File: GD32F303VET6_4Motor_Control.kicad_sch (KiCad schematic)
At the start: 0 parts

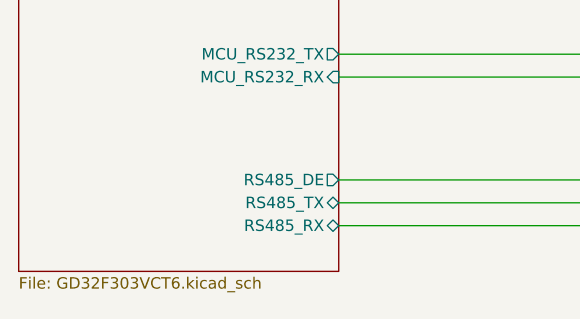
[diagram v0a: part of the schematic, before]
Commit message: 重命名为GD32F303VET6四电机驱动控制板
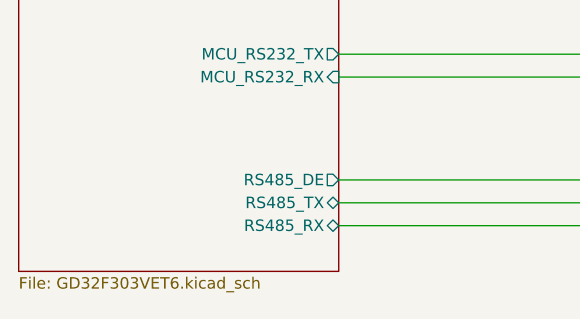
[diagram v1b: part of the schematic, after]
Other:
- sheet MCU_Core: file GD32F303VCT6.kicad_sch -> GD32F303VET6.kicad_sch
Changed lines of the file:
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@@
 		)
 		(instances
-			(project "GD32F303"
+			(project "GD32F303VET6_4Motor_Control"
 				(path "/54005433-e3aa-4693-8f75-bb73943288d3"
 					(page "6")
@@
 		)
 		(instances
-			(project "GD32F303"
+			(project "GD32F303VET6_4Motor_Control"
 				(path "/54005433-e3aa-4693-8f75-bb73943288d3"
 					(page "4")
@@
 		)
 		(instances
-			(project "GD32F303"
+			(project "GD32F303VET6_4Motor_Control"
 				(path "/54005433-e3aa-4693-8f75-bb73943288d3"
 					(page "5")
@@
 		)
 		(instances
-			(project "GD32F303"
+			(project "GD32F303VET6_4Motor_Control"
 				(path "/54005433-e3aa-4693-8f75-bb73943288d3"
 					(page "2")
@@
 			)
 		)
-		(property "Sheetfile" "GD32F303VCT6.kicad_sch"
+		(property "Sheetfile" "GD32F303VET6.kicad_sch"
 			(at 128.27 149.1746 0)
 			(show_name no)
@@
 		)
 		(instances
-			(project "GD32F303"
+			(project "GD32F303VET6_4Motor_Control"
 				(path "/54005433-e3aa-4693-8f75-bb73943288d3"
 					(page "3")

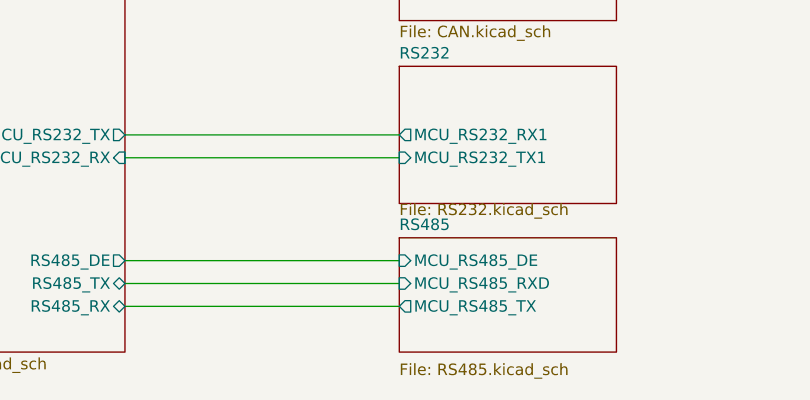
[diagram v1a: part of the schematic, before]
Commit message: 更新六层电机控制板设计与器件库
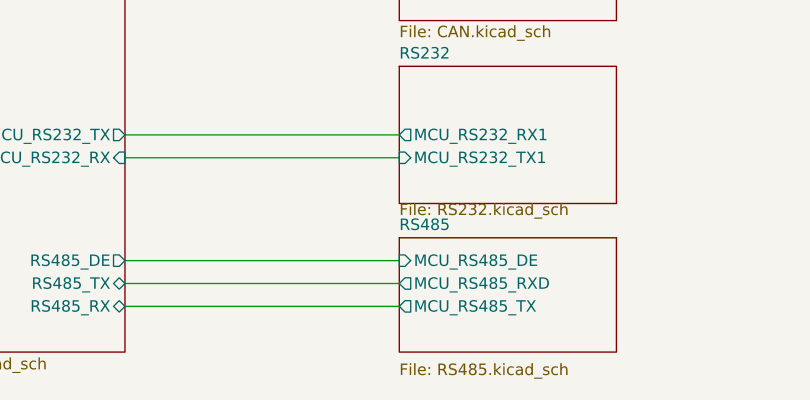
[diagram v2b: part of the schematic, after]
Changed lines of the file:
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@@
 			)
 		)
-		(pin "MCU_RS485_RXD" input
+		(pin "MCU_RS485_RXD" output
 			(at 194.31 140.97 180)
 			(effects

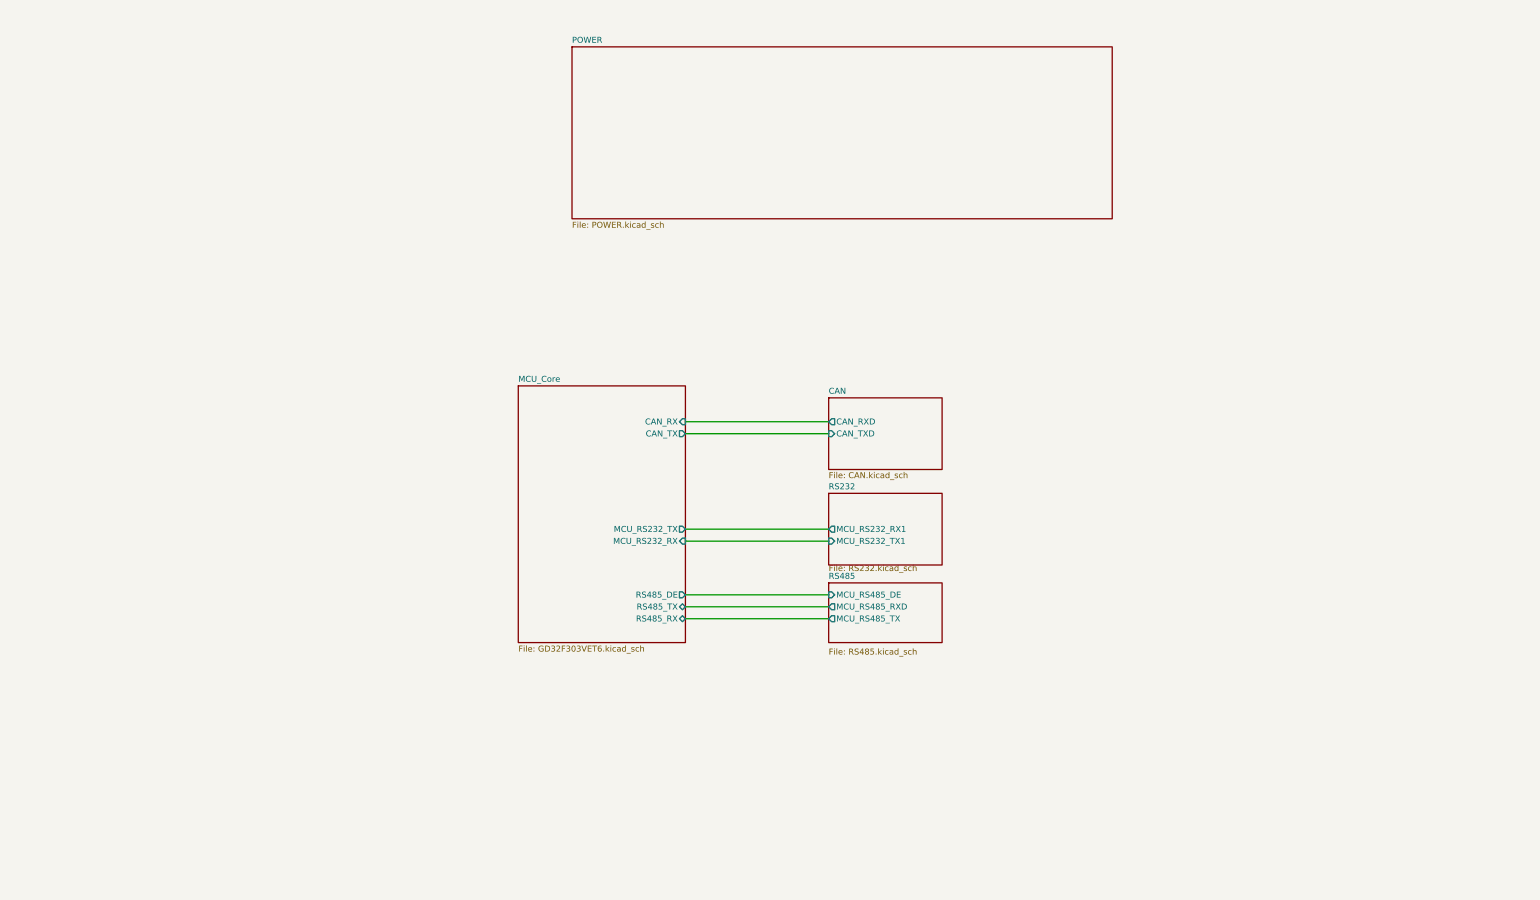
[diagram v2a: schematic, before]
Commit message: V2.0: sync KiCad design, add firmware snapshot and README
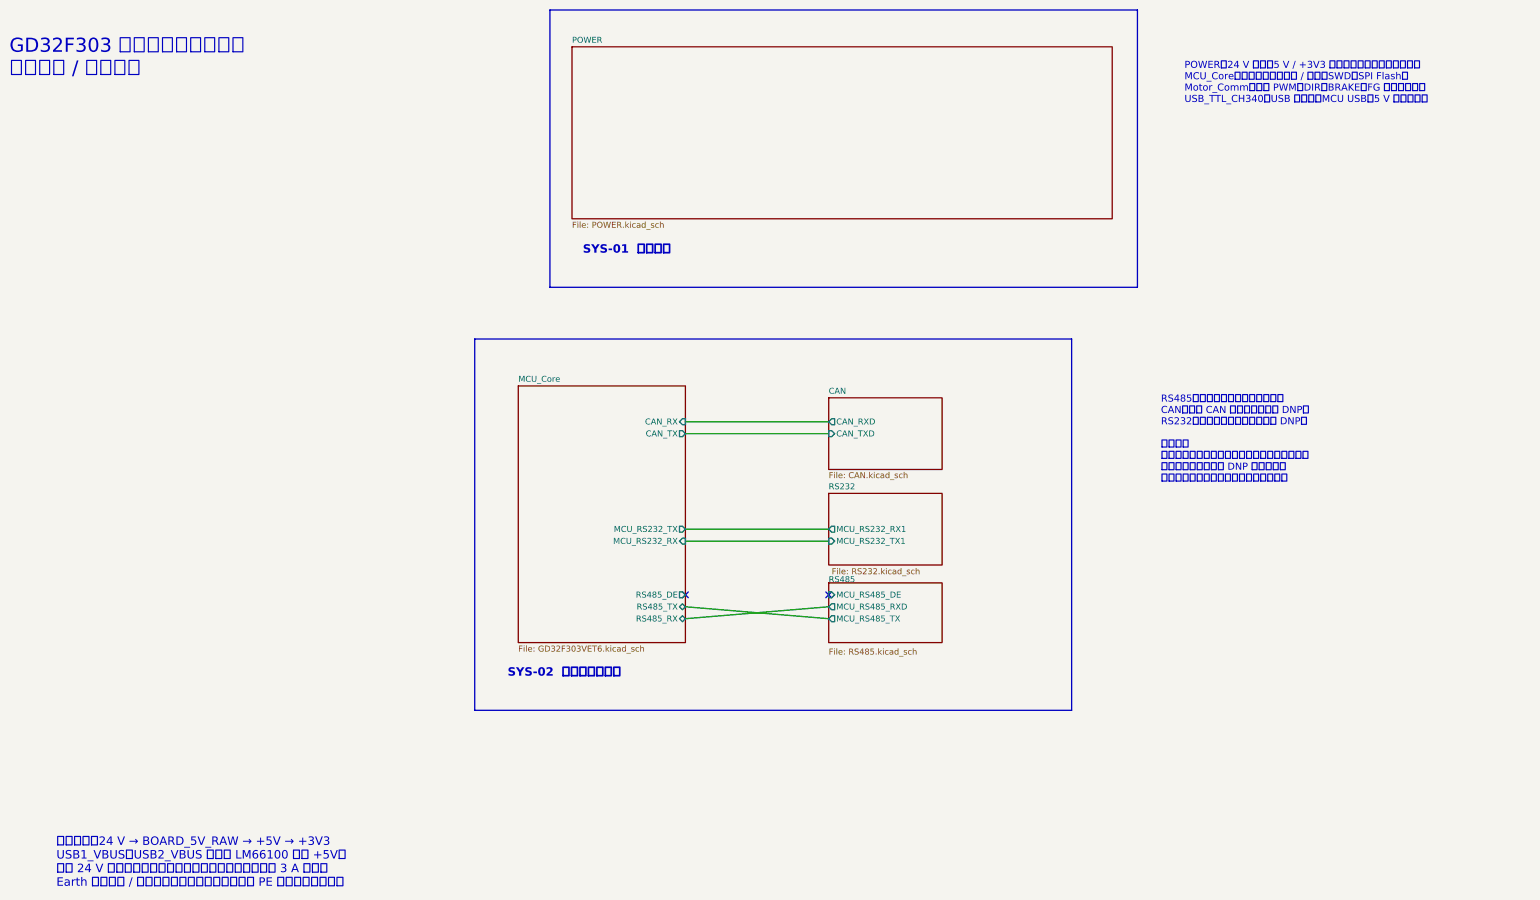
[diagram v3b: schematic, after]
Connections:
- no-connect marks 0 -> 2
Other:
- note added: "GD32F303 四路无刷电机控制板 系统总览 / 功能分区"
- note added: "POWER：24 V 输入、5 V / +3V3 电源、供电指示、机壳连接。 MCU_Core：主控、时钟、启动 / 复位、SWD、SPI Flash。 Motor_Comm：四路 PWM、DIR、BRAKE、FG 与电机接口。 USB_TTL_CH340：USB 转串口、MCU USB、5 V 电源汇合。"
- note added: "RS485：当前装配的自动收发接口。 CAN：隔离 CAN 备用电路，当前 DNP。 RS232：电平转换备用电路，当前 DNP。 阅读约定 实线框：功能分区；虚线框：备用不装配区域。 具体装配状态以元件 DNP 属性为准。 分区编号仅用于阅读，不改变网络连接。"
- note added: "SYS-01 电源系统"
- note added: "SYS-02 主控与通信互联"
- note added: "供电路径：24 V → BOARD_5V_RAW → +5V → +3V3 USB1_VBUS、USB2_VBUS 经各自 LM66100 接入 +5V。 电机 24 V 回路与控制板共地；四路电机合计最大电流按 3 A 设计。 Earth 表示机壳 / 金属安装板网络，是否接保护地 PE 由整机接线决定。"
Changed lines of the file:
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@@
 	(generator_version "10.0")
 	(paper "A3")
-	(wire
-		(pts
-			(xy 163.83 143.51) (xy 194.31 143.51)
-		)
-		(stroke
-			(width 0)
-			(type default)
-		)
+	(rectangle
+		(start 135 14)
+		(end 260 73)
+		(stroke
+			(width 0.254)
+			(type solid)
+		)
+		(fill
+			(type none)
+		)
+	)
+	(rectangle
+		(start 119 84)
+		(end 246 163)
+		(stroke
+			(width 0.254)
+			(type solid)
+		)
+		(fill
+			(type none)
+		)
+	)
+	(text "GD32F303 四路无刷电机控制板\n系统总览 / 功能分区"
+		(exclude_from_sim no)
+		(at 20 20 0)
+		(effects
+			(font
+				(face "宋体")
+				(size 3 3)
+			)
+			(justify left top)
+		)
+	)
+	(text "SYS-02  主控与通信互联"
+		(exclude_from_sim no)
+		(at 126 154 0)
+		(effects
+			(font
+				(face "宋体")
+				(size 1.8 1.8)
+				(bold yes)
+			)
+			(justify left top)
+		)
+	)
+	(text "供电路径：24 V → BOARD_5V_RAW → +5V → +3V3\nUSB1_VBUS、USB2_VBUS 经各自 LM66100 接入 +5V。\n电机 24 V 回路与控制板共地；四路电机合计最大电流按 3 A 设计。\nEarth 表示机壳 / 金属安装板网络，是否接保护地 PE 由整机接线决定。"
+		(exclude_from_sim no)
+		(at 30 190 0)
+		(effects
+			(font
+				(face "宋体")
+				(size 1.8 1.8)
+			)
+			(justify left top)
+		)
+	)
+	(text "POWER：24 V 输入、5 V / +3V3 电源、供电指示、机壳连接。\nMCU_Core：主控、时钟、启动 / 复位、SWD、SPI Flash。\nMotor_Comm：四路 PWM、DIR、BRAKE、FG 与电机接口。\nUSB_TTL_CH340：USB 转串口、MCU USB、5 V 电源汇合。"
+		(exclude_from_sim no)
+		(at 270 25 0)
+		(effects
+			(font
+				(face "宋体")
+				(size 1.5 1.5)
+			)
+			(justify left top)
+		)
+	)
+	(text "SYS-01  电源系统"
+		(exclude_from_sim no)
+		(at 142 64 0)
+		(effects
+			(font
+				(face "宋体")
+				(size 1.8 1.8)
+				(bold yes)
+			)
+			(justify left top)
+		)
+	)
+	(text "RS485：当前装配的自动收发接口。\nCAN：隔离 CAN 备用电路，当前 DNP。\nRS232：电平转换备用电路，当前 DNP。\n\n阅读约定\n实线框：功能分区；虚线框：备用不装配区域。\n具体装配状态以元件 DNP 属性为准。\n分区编号仅用于阅读，不改变网络连接。"
+		(exclude_from_sim no)
+		(at 265 96 0)
+		(effects
+			(font
+				(face "宋体")
+				(size 1.5 1.5)
+			)
+			(justify left top)
+		)
+	)
+	(no_connect
+		(at 163.83 138.43)
+	)
+	(no_connect
+		(at 194.31 138.43)
 	)
 	(wire
@@
 	(wire
 		(pts
+			(xy 194.31 140.97) (xy 163.83 143.51)
+		)
+		(stroke
+			(width 0)
+			(type default)
+		)
+	)
+	(wire
+		(pts
 			(xy 194.31 101.6) (xy 163.83 101.6)
 		)
@@
 	(wire
 		(pts
-			(xy 163.83 140.97) (xy 194.31 140.97)
-		)
-		(stroke
-			(width 0)
-			(type default)
-		)
-	)
-	(wire
-		(pts
 			(xy 163.83 104.14) (xy 194.31 104.14)
 		)
@@
 	(wire
 		(pts
-			(xy 163.83 138.43) (xy 194.31 138.43)
+			(xy 163.83 140.97) (xy 194.31 143.51)
 		)
 		(stroke
@@
 		(on_board yes)
 		(dnp no)
-		(fields_autoplaced yes)
 		(stroke
 			(width 0.1524)
@@
 		)
 		(property "Sheetname" "RS485"
-			(at 194.31 135.1784 0)
+			(at 194.31 135.89 0)
 			(show_name no)
 			(do_not_autoplace no)
@@
 		(on_board yes)
 		(dnp no)
-		(fields_autoplaced yes)
 		(stroke
 			(width 0.1524)
@@
 		)
 		(property "Sheetfile" "RS232.kicad_sch"
-			(at 194.31 132.0296 0)
-			(show_name no)
-			(do_not_autoplace no)
+			(at 194.945 132.715 0)
+			(show_name no)
+			(do_not_autoplace no)

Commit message: 更新V2.0电路设计及0.5oz内层制造交付资料
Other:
- note added: "24V → BOARD_5V_RAW → +5V → +3V3。 USB1_VBUS / USB2_VBUS 经各自 LM66100 汇入 +5V。 四路电机合计最大电流按 3A；控制与电机共地。 Earth 为机壳 / 金属安装板网络，是否连接 PE 由整机接线决定。"
- note added: "GD32F303 四路电机控制板 系统功能目录"
- note added: "POWER：24V 输入、5V / 3V3、电源指示、Earth。 MCU_Core：主控、时钟、复位、SWD、SPI Flash。 Motor_Comm：四路 PWM、DIR、BRAKE、FG。 新增 MOT-08：PA15 可编程 LED，低电平亮。 USB_TTL_CH340：串口桥、原生 USB、供电汇合。 CH340 使用 USART2：PD8 TX / PD9 RX。 RS485：USART1 自动收发，共地接口。 CAN / RS232：保留电路，当前不装配。 WiFi_OTA：备用不装配，USART0 / PA9、PA10。 实线：功能分区；虚线：备用 DNP。 具体装配及 PCB 排除状态以元件属性为准。 注释说明当前接线，不代表电气验收通过。"
- note added: "SYS-02 主控与总线接口"
- note added: "SYS-03 功能目录与装配状态"
- note added: "SYS-04 供电与接地路径"
- note removed: "GD32F303 四路无刷电机控制板 系统总览 / 功能分区"
- note removed: "POWER：24 V 输入、5 V / +3V3 电源、供电指示、机壳连接。 MCU_Core：主控、时钟、启动 / 复位、SWD、SPI Flash。 Motor_Comm：四路 PWM、DIR、BRAKE、FG 与电机接口。 USB_TTL_CH340：USB 转串口、MCU USB、5 V 电源汇合。"
- note removed: "RS485：当前装配的自动收发接口。 CAN：隔离 CAN 备用电路，当前 DNP。 RS232：电平转换备用电路，当前 DNP。 阅读约定 实线框：功能分区；虚线框：备用不装配区域。 具体装配状态以元件 DNP 属性为准。 分区编号仅用于阅读，不改变网络连接。"
- note removed: "SYS-02 主控与通信互联"
- note removed: "供电路径：24 V → BOARD_5V_RAW → +5V → +3V3 USB1_VBUS、USB2_VBUS 经各自 LM66100 接入 +5V。 电机 24 V 回路与控制板共地；四路电机合计最大电流按 3 A 设计。 Earth 表示机壳 / 金属安装板网络，是否接保护地 PE 由整机接线决定。"
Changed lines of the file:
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@@
+	)
+	(rectangle
+		(start 20 175)
+		(end 265 221)
+		(stroke
+			(width 0.254)
+			(type solid)
+		)
+		(fill
+			(type none)
+		)
 	)
 	(rectangle
@@
 		)
 	)
-	(text "GD32F303 四路无刷电机控制板\n系统总览 / 功能分区"
+	(rectangle
+		(start 265 14)
+		(end 405 164)
+		(stroke
+			(width 0.254)
+			(type solid)
+		)
+		(fill
+			(type none)
+		)
+	)
+	(text "POWER：24V 输入、5V / 3V3、电源指示、Earth。\nMCU_Core：主控、时钟、复位、SWD、SPI Flash。\nMotor_Comm：四路 PWM、DIR、BRAKE、FG。\n新增 MOT-08：PA15 可编程 LED，低电平亮。\nUSB_TTL_CH340：串口桥、原生 USB、供电汇合。\nCH340 使用 USART2：PD8 TX / PD9 RX。\nRS485：USART1 自动收发，共地接口。\nCAN / RS232：保留电路，当前不装配。\nWiFi_OTA：备用不装配，USART0 / PA9、PA10。\n\n实线：功能分区；虚线：备用 DNP。\n具体装配及 PCB 排除状态以元件属性为准。\n注释说明当前接线，不代表电气验收通过。"
 		(exclude_from_sim no)
-		(at 20 20 0)
+		(at 270 27 0)
 		(effects
 			(font
-				(face "宋体")
-				(size 3 3)
+				(face "Microsoft YaHei")
+				(size 1.8 1.8)
 			)
 			(justify left top)
 		)
 	)
-	(text "SYS-02  主控与通信互联"
+	(text "SYS-04  供电与接地路径"
 		(exclude_from_sim no)
-		(at 126 154 0)
+		(at 23 178 0)
 		(effects
 			(font
-				(face "宋体")
-				(size 1.8 1.8)
+				(face "Microsoft YaHei")
+				(size 2 2)
 				(bold yes)
 			)
@@
 		)
 	)
-	(text "供电路径：24 V → BOARD_5V_RAW → +5V → +3V3\nUSB1_VBUS、USB2_VBUS 经各自 LM66100 接入 +5V。\n电机 24 V 回路与控制板共地；四路电机合计最大电流按 3 A 设计。\nEarth 表示机壳 / 金属安装板网络，是否接保护地 PE 由整机接线决定。"
+	(text "24V → BOARD_5V_RAW → +5V → +3V3。\nUSB1_VBUS / USB2_VBUS 经各自 LM66100 汇入 +5V。\n四路电机合计最大电流按 3A；控制与电机共地。\nEarth 为机壳 / 金属安装板网络，是否连接 PE 由整机接线决定。"
 		(exclude_from_sim no)
-		(at 30 190 0)
+		(at 25 187 0)
 		(effects
 			(font
-				(face "宋体")
+				(face "Microsoft YaHei")
 				(size 1.8 1.8)
-			)
-			(justify left top)
-		)
-	)
-	(text "POWER：24 V 输入、5 V / +3V3 电源、供电指示、机壳连接。\nMCU_Core：主控、时钟、启动 / 复位、SWD、SPI Flash。\nMotor_Comm：四路 PWM、DIR、BRAKE、FG 与电机接口。\nUSB_TTL_CH340：USB 转串口、MCU USB、5 V 电源汇合。"
-		(exclude_from_sim no)
-		(at 270 25 0)
-		(effects
-			(font
-				(face "宋体")
-				(size 1.5 1.5)
 			)
 			(justify left top)
@@
 	(text "SYS-01  电源系统"
 		(exclude_from_sim no)
-		(at 142 64 0)
+		(at 141 64 0)
 		(effects
 			(font
-				(face "宋体")
-				(size 1.8 1.8)
+				(face "Microsoft YaHei")
+				(size 2 2)
 				(bold yes)
 			)
@@
 		)
 	)
-	(text "RS485：当前装配的自动收发接口。\nCAN：隔离 CAN 备用电路，当前 DNP。\nRS232：电平转换备用电路，当前 DNP。\n\n阅读约定\n实线框：功能分区；虚线框：备用不装配区域。\n具体装配状态以元件 DNP 属性为准。\n分区编号仅用于阅读，不改变网络连接。"
+	(text "SYS-02  主控与总线接口"
 		(exclude_from_sim no)
-		(at 265 96 0)
+		(at 125 154 0)
 		(effects
 			(font
-				(face "宋体")
-				(size 1.5 1.5)
+				(face "Microsoft YaHei")
+				(size 2 2)
+				(bold yes)
 			)
 			(justify left top)
+		)
+	)
+	(text "SYS-03  功能目录与装配状态"
+		(exclude_from_sim no)
+		(at 268 17 0)
+		(effects
+			(font
+				(face "Microsoft YaHei")
+				(size 2 2)
+				(bold yes)
+			)
+			(justify left top)
+		)
+	)
+	(text "GD32F303 四路电机控制板\n系统功能目录"
+		(exclude_from_sim no)
+		(at 20 20 0)
+		(effects
+			(font
+				(face "Microsoft YaHei")
+				(size 3 3)
+			)
+			(justify left top)
